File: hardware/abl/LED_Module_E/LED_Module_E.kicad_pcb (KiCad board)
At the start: 4 copper layers, 140.8 x 26 mm, 93 parts, among them J1 SFW20S-2STE1LF, J3 009159008603906, Q1 Si3456DDV, Q11 Si3456DDV, Q12 Si3456DDV, Q2 Si3456DDV, Q3 Si3456DDV, Q4 Si3456DDV, Q5 Si3456DDV, Q6 Si3456DDV, Q7 Si3456DDV, Q8 Si3456DDV, U1 TMP1075DGK, U2 74HCT244, U3 24AA02UIDT-I/OT

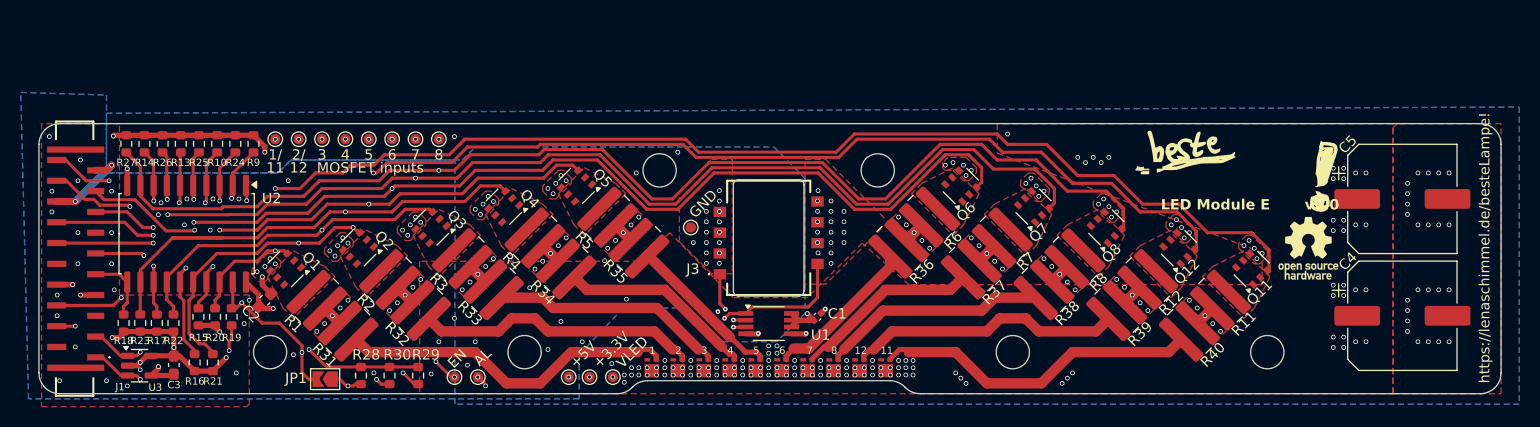
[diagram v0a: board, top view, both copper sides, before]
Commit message: Implemented a lot of recommended changes, including layer swap.
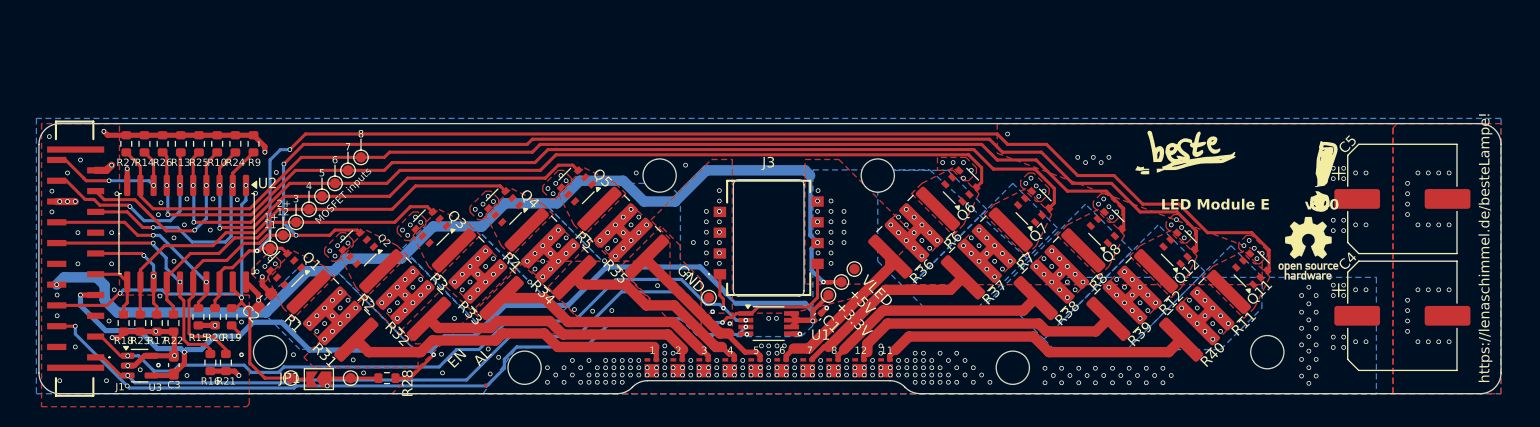
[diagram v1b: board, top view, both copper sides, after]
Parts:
- removed R29, R30: 2740R, Resistor_SMD:R_0603_1608Metric
- C1, C2, C3: value 10nF -> 100nF
- R1, R11, R12, R2, R3, R31, R32, R33, R34, R35, R36, R37, R38, R39, R4, R40, R5, R6, R7, R8: value 220mR -> 200mR
- R10, R13, R14, R15, R16, R17, R18, R20, R21, R22, R23, R24, R25, R26, R27, R9: value 2740R -> 4700R
- moved TP4 27.8 mm to (144.5, 72.2)
- moved TP3 25.5 mm to (145.8, 71.0)
- moved TP2 24.3 mm to (143.2, 73.5)
- moved TP6 15.8 mm to (91.5, 81.5)
- moved TP5 12.3 mm to (97.2, 81.5)
- moved TP7 10.5 mm to (89.5, 69.0)
- moved TP8 9.37 mm to (90.8, 67.8)
- moved TP9 8.38 mm to (92.0, 66.5)
- moved TP14 7.70 mm to (98.2, 60.2)
- moved TP10 7.60 mm to (93.2, 65.2)
- moved TP13 7.16 mm to (97.0, 61.5)
- moved TP11 7.11 mm to (94.5, 64.0)
- moved TP1 6.97 mm to (131.8, 73.8)
- moved TP12 6.95 mm to (95.8, 62.8)
- moved R28 2.51 mm to (100.8, 81.5), turned to 180 degrees
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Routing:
- net +3.3V: track 120.3 -> 102.7 mm, vias 7 -> 5
- net /ENABLE: track 61.1 -> 46.3 mm, vias 6 -> 3
- net +5V: track 111.6 -> 97.9 mm, vias 5 -> 4
- net Net-(Q4-G): track 54.9 -> 43.0 mm, vias 2 -> 0
- net Net-(Q6-G): track 99.7 -> 88.1 mm, vias 4 -> 2
- net Net-(Q7-G): track 108.4 -> 97.8 mm, vias 4 -> 2
- net Net-(Q8-G): track 116.9 -> 107.1 mm, vias 2 -> 0
- net Net-(Q3-G): track 41.0 -> 32.5 mm, vias 2 -> 0
- net Net-(Q5-G): track 52.4 -> 45.2 mm, vias 4 -> 2
- net +4V: track 8.49 -> 3.54 mm, vias 142 -> 241
- net GND: track 44.6 -> 39.9 mm, vias 144 -> 157
- net /SCL: track 76.9 -> 73.3 mm, vias 4 -> 3
- net Net-(Q1-G): track 127.8 -> 125.1 mm, vias 3 -> 2
- net /SDA: track 82.4 -> 79.6 mm, vias 3 -> 2
- net /i4: track 16.0 -> 13.9 mm
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- added copper zone on F.Cu, net Net-(D1-K)
- added copper zone on F.Cu, net Net-(D2-K)
- added copper zone on F.Cu, net Net-(D3-K)
- added copper zone on F.Cu, net Net-(D4-K)
- added copper zone on F.Cu, net Net-(D5-K)
- added copper zone on B.Cu, net Net-(R1-Pad1)
- added copper zone on B.Cu, net Net-(R11-Pad1)
- added copper zone on B.Cu, net Net-(R12-Pad1)
- added copper zone on B.Cu, net Net-(R2-Pad1)
- added copper zone on B.Cu, net Net-(R3-Pad1)
- added copper zone on B.Cu, net Net-(R34-Pad2)
- added copper zone on B.Cu, net Net-(R35-Pad2)
- added copper zone on B.Cu, net Net-(R36-Pad2)
- added copper zone on B.Cu, net Net-(R37-Pad2)
- added copper zone on B.Cu, net Net-(R38-Pad2)
- removed copper zone on In2.Cu, net Net-(R1-Pad1)
- removed copper zone on In2.Cu, net Net-(R11-Pad1)
- removed copper zone on In2.Cu, net Net-(R12-Pad1)
- removed copper zone on In2.Cu, net Net-(R2-Pad1)
- removed copper zone on In2.Cu, net Net-(R3-Pad1)
- removed copper zone on In2.Cu, net Net-(R34-Pad2)
- removed copper zone on In2.Cu, net Net-(R35-Pad2)
- removed copper zone on In2.Cu, net Net-(R36-Pad2)
- removed copper zone on In2.Cu, net Net-(R37-Pad2)
- removed copper zone on In2.Cu, net Net-(R38-Pad2)
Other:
- board text added: "1+"
- board text added: "2+"
- board text removed: "1/"
- board text removed: "2/"

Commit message: Changed driver, mirrored LEDs and general cleanup.
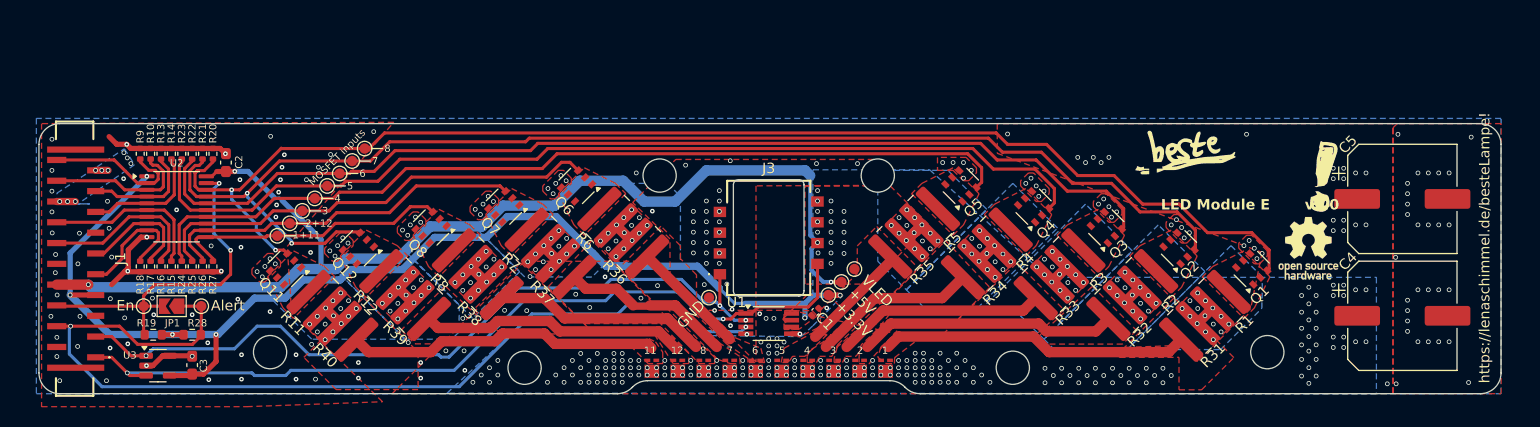
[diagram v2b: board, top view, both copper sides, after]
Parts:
- R10, R13, R14, R15, R16, R17, R18, R20, R21, R22, R23, R24, R25, R26, R27, R9: footprint Resistor_SMD:R_0603_1608Metric -> Resistor_SMD:R_0402_1005Metric
- U2: value 74HCT244 -> 74HC245; footprint Package_SO:SOIC-20W_7.5x12.8mm_P1.27mm -> Package_SO:TSSOP-20_4.4x6.5mm_P0.65mm
- moved Q1 93.0 mm to (184.0, 71.0), turned to 135 degrees
- moved Q11 93.0 mm to (91.0, 71.0), turned to -135 degrees
- moved R1 87.0 mm to (181.0, 74.0), turned to 45 degrees
- moved R11 87.0 mm to (94.0, 74.0), turned to 135 degrees
- moved R31 81.0 mm to (178.0, 77.0), turned to 45 degrees
- moved R40 81.0 mm to (97.0, 77.0), turned to 135 degrees
- moved Q12 79.0 mm to (98.0, 69.0), turned to -135 degrees
- moved Q2 79.0 mm to (177.0, 69.0), turned to 135 degrees
- moved R12 73.0 mm to (101.0, 72.0), turned to 135 degrees
- moved R2 73.0 mm to (174.0, 72.0), turned to 45 degrees
- moved R32 67.0 mm to (171.0, 75.0), turned to 45 degrees
- moved R39 67.0 mm to (104.0, 75.0), turned to 135 degrees
- moved Q3 65.0 mm to (170.0, 67.0), turned to 135 degrees
- moved Q8 65.0 mm to (105.0, 67.0), turned to -135 degrees
- moved R3 59.0 mm to (167.0, 70.0), turned to 45 degrees
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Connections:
- J1 pad 15: /i1 -> /i4
- J1 pad 17: /i2 -> /i3
- J1 pad 18: /i3 -> /i2
- J1 pad 20: /i4 -> /i1
- U2 pad 1: /ENABLE -> +3.3V
- U2 pad 11: /i8 -> Net-(Q8-G)
- U2 pad 12: Net-(Q4-G) -> Net-(Q7-G)
- U2 pad 13: /i7 -> Net-(Q6-G)
- U2 pad 14: Net-(Q3-G) -> Net-(Q5-G)
- U2 pad 15: /i6 -> Net-(Q4-G)
- U2 pad 16: Net-(Q12-G) -> Net-(Q3-G)
- U2 pad 17: /i5 -> Net-(Q12-G)
- U2 pad 3: Net-(Q5-G) -> /i2
- U2 pad 4: /i2 -> /i3
- U2 pad 5: Net-(Q6-G) -> /i4
- U2 pad 6: /i3 -> /i5
- U2 pad 7: Net-(Q7-G) -> /i6
- U2 pad 8: /i4 -> /i7
- U2 pad 9: Net-(Q8-G) -> /i8
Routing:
- net Net-(Q8-G): track 107.1 -> 27.1 mm
- net Net-(Q3-G): track 32.5 -> 101.5 mm
- net Net-(Q7-G): track 97.8 -> 35.6 mm, vias 2 -> 0
- net Net-(Q4-G): track 43.0 -> 94.8 mm
- net Net-(Q6-G): track 88.1 -> 44.2 mm, vias 2 -> 0
- net Net-(Q5-G): track 45.2 -> 86.3 mm, vias 2 -> 0
- net +3.3V: track 102.7 -> 124.2 mm, vias 5 -> 6
- net /ALERT: track 78.6 -> 93.8 mm, vias 4 -> 2
- net /ENABLE: track 46.3 -> 34.2 mm, vias 3 -> 2
- net +5V: track 97.9 -> 109.1 mm
- net /i1: track 23.4 -> 13.9 mm, vias 2 -> 0
- net /i3: track 19.5 -> 10.9 mm, vias 2 -> 0
- net Net-(Q12-G): track 130.3 -> 122.4 mm
- net /i6: track 23.2 -> 16.0 mm, vias 2 -> 0
- net GND: track 39.9 -> 33.2 mm, vias 157 -> 193
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- added copper zone on F.Cu, net +3.3V
- added copper zone on F.Cu, net Net-(D11-K)
- added copper zone on F.Cu, net Net-(D12-K)
- added copper zone on F.Cu, net Net-(D6-K)
- added copper zone on F.Cu, net Net-(D7-K)
- added copper zone on F.Cu, net Net-(D8-K)
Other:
- board text added: "1+11"
- board text added: "2+12"
- board text added: "Alert"
- board text added: "En"
- board text removed: "1+"
- board text removed: "2+"
- board text removed: "AL"
- board text removed: "EN"

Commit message: Re-numbered resistors.
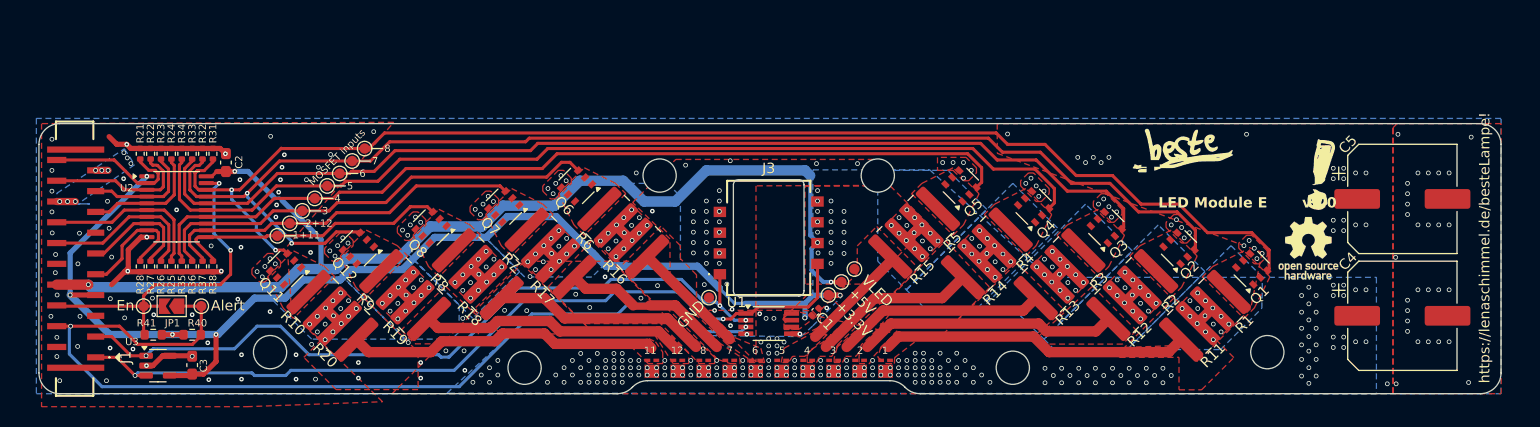
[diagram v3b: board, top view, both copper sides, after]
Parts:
- moved G*** 0.31 mm to (182.5, 61.3)
- renumbered R11 to R10, R31 to R11, R32 to R12, R33 to R13, R34 to R14, R35 to R15, R36 to R16, R37 to R17, R38 to R18, R39 to R19, R40 to R20, R9 to R21, R10 to R22, R13 to R23, R14 to R24, R15 to R25, R16 to R26, R17 to R27, R18 to R28, R20 to R31, R21 to R32, R22 to R33, R23 to R34, R24 to R35, R25 to R36, R26 to R37, R27 to R38, R28 to R40, R19 to R41, R12 to R9
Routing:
- net /SDA: track 80.7 -> 80.0 mm

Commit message: Fixed a few footprints and part numbers.
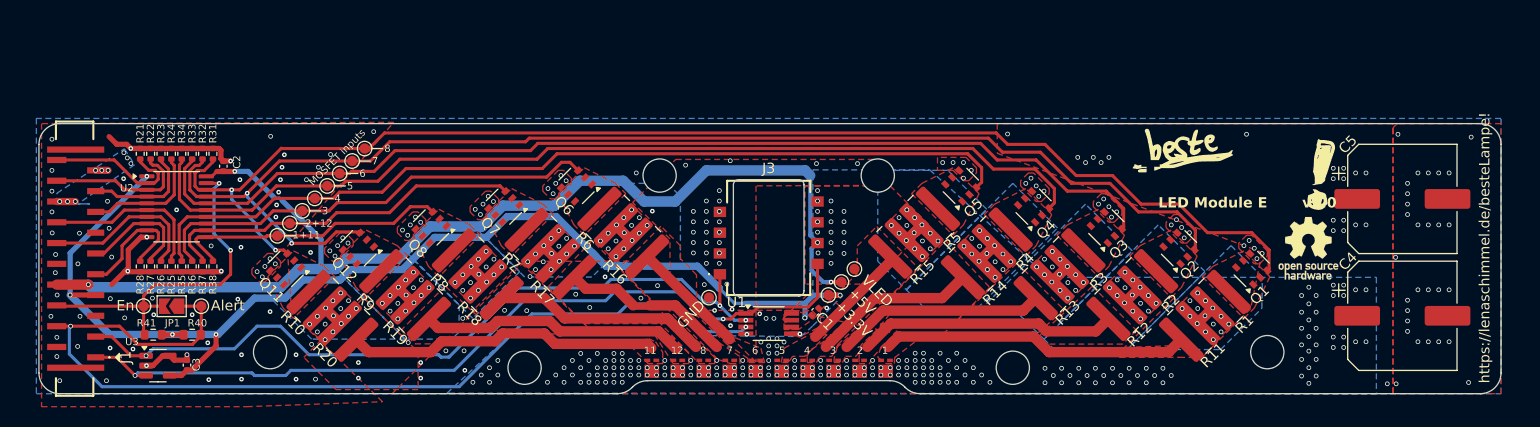
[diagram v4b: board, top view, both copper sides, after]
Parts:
- C2, C3: footprint Capacitor_SMD:C_0603_1608Metric_Pad1.08x0.95mm_HandSolder -> Capacitor_SMD:C_0402_1005Metric
- moved C3 0.50 mm to (81.5, 80.2)
- moved C2 0.43 mm to (85.0, 61.1)
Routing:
- net GND: track 33.2 -> 34.7 mm
- net +3.3V: track 124.2 -> 123.3 mm

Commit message: Fix DRC errors and do some finishing touches.
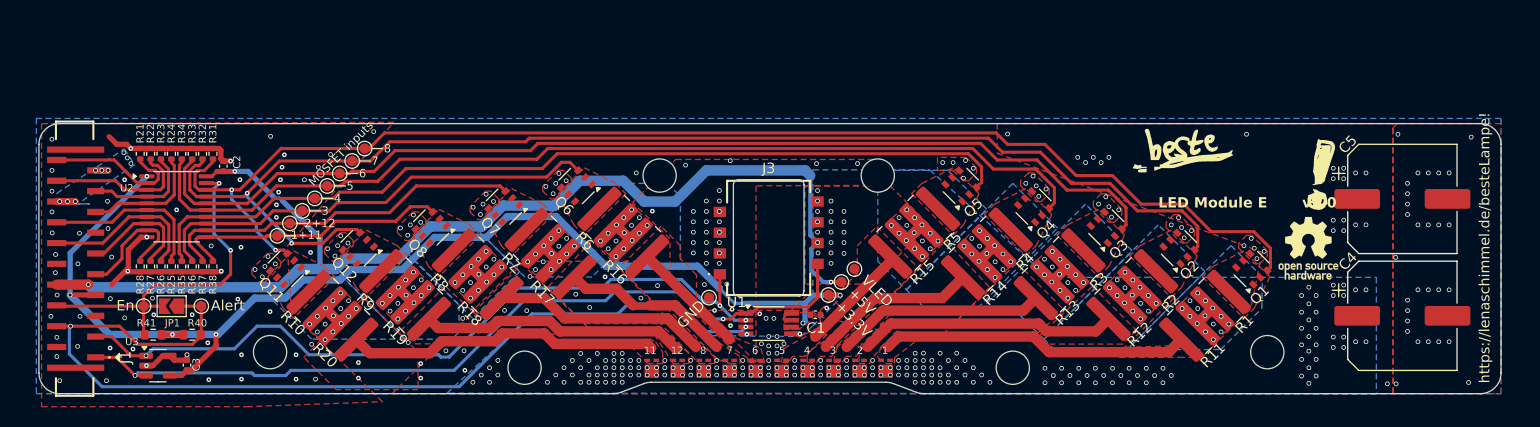
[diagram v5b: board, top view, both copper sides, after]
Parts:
- moved C1 0.28 mm to (142.0, 75.4), turned to 180 degrees
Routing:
- net Net-(Q12-G): track 122.4 -> 123.1 mm
- net GND: vias 193 -> 195
- net (no net): vias 2 -> 0
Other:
- outline, holes or cut-outs redrawn

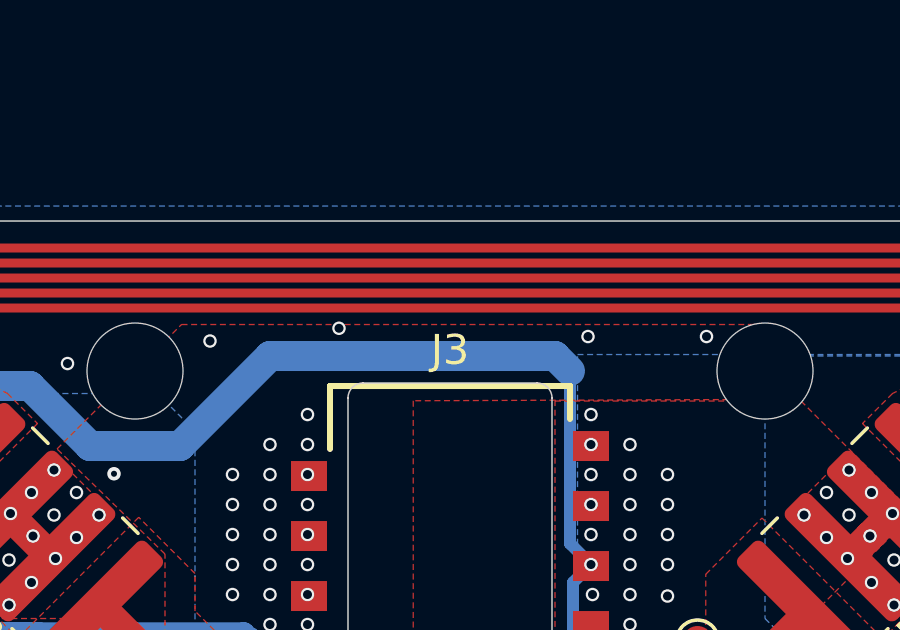
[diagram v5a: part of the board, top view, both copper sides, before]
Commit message: Add current renderings to all ABL PCBs.
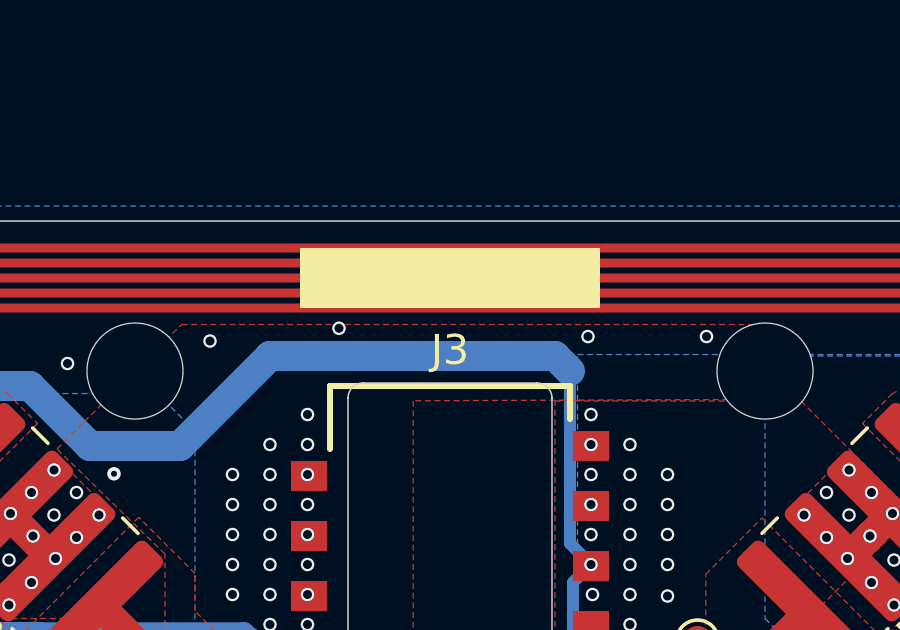
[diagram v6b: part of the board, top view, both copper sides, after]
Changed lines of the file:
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@@
 					(face "Podkova")
 					(size 1 1)
-					(thickness 0.254)
+					(thickness 0.25)
 				)
 			)
@@
 			)
 		)
-		(sheetname "Root")
-		(sheetfile "LED_Module_E.kicad_sch")
 		(attr smd)
 		(fp_line
@@
 		(model "009159008603906.stp"
 			(offset
-				(xyz 0 0 0)
+				(xyz 0 0 -4.475)
 			)
 			(scale
@@
 			)
 			(rotate
-				(xyz 0 0 0)
+				(xyz 180 0 0)
 			)
 		)
@@
 		(layer "F.SilkS")
 	)
+	(gr_rect
+		(start 132.5 57.9)
+		(end 142.5 59.9)
+		(stroke
+			(width 0)
+			(type default)
+		)
+		(fill solid)
+		(layer "F.SilkS")
+	)

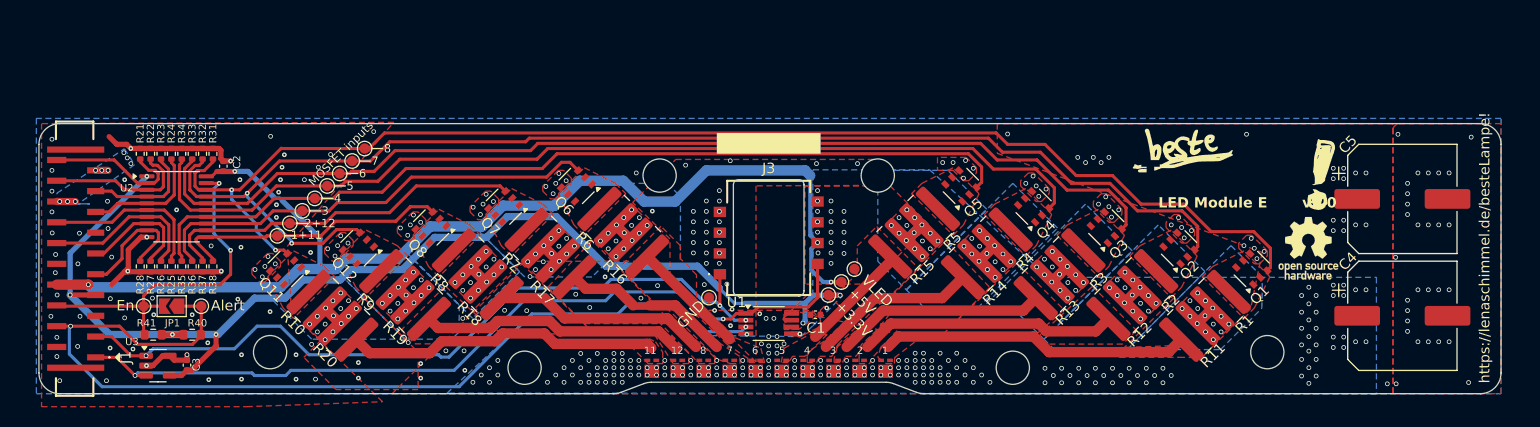
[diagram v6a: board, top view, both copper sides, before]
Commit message: Added an EEPROM to the power module and changed the EEPROM on the LED module to be individually addressable.
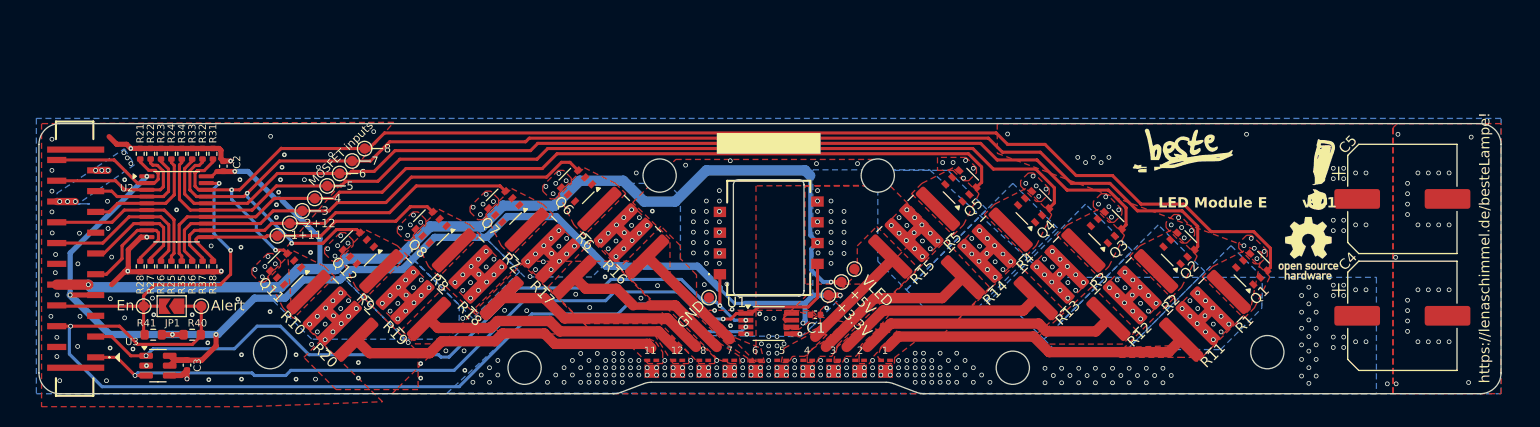
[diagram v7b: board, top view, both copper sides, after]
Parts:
- U3: value 24AA02UIDT-I/OT -> 24AA025UIDT-I/OT; footprint Package_TO_SOT_SMD:SOT-23-5 -> Package_TO_SOT_SMD:SOT-23-6
- turned C3 to 90 degrees
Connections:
- U3 pad 4: +3.3V -> GND
- U3 pad 5: GND -> +3.3V
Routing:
- net GND: track 34.7 -> 32.4 mm
- net +3.3V: track 123.4 -> 124.9 mm
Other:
- board text added: "LED Module E v2.1"
- board text removed: "LED Module E v2.0"
